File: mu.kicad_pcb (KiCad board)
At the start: 4 copper layers, 60 x 60 mm, 80 parts, among them J1 JTAG-10 PIN, J2 XT30PW-M, J5 ESQ-110-X-X-D, U1 STM32F042F6P6, U10 TLV3603QDCKRQ1, U11 SN74LVC1G74DCUT, U12 LM4040AIM3-2.5/NOPB, U13 MCP4921-E/SN, U14 BMP390, U2 MAX5026EUT_T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

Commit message: fixed the connector
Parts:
- removed C32: 100nF, Resistor_SMD:R_0402_1005Metric
- removed R16: 2.49KΩ 0.1%, Resistor_SMD:R_0402_1005Metric
- removed U12: LM4040AIM3-2.5/NOPB, footprints:DBZ3
- added J3: U.FL-R-SMT-1_10_, footprints:HRS_U.FL-R-SMT-1_10_, B.Cu at (159.2, 75.0)
- added R7: 0Ω, Resistor_SMD:R_0402_1005Metric, B.Cu at (154.0, 73.0)
- added R8: 50Ω 0.1%, Resistor_SMD:R_0402_1005Metric, B.Cu at (156.0, 72.9)
- R1: value 220K -> 210K
- moved R3 0.37 mm to (154.8, 74.8)
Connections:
- J2 pad N: Net-(MOSFET1-D) -> GND
- J2 pad P: GND -> Net-(MOSFET1-D)
- J5 pad 01: 5v_SERVO -> unconnected-(J5-Pad01)
- J5 pad 02: 5v_SERVO -> unconnected-(J5-Pad02)
- J5 pad 09: NRST1 -> unconnected-(J5-Pad09)
- J5 pad 10: NRST2 -> unconnected-(J5-Pad10)
- J5 pad 11: NRST3 -> unconnected-(J5-Pad11)
- J5 pad 12: NRST4 -> unconnected-(J5-Pad12)
- J5 pad 13: NRST5 -> unconnected-(J5-Pad13)
- R3 pad 1: 2.5V_Ref -> GND
- Rg1 pad 2: 2.5V_Ref -> GND
- U3 pad 1: 2.5V_Ref -> GND
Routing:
- net 2.5V_Ref: track 12.5 -> 0.00 mm, vias 1 -> 0
- net Net-(MOSFET1-D): track 13.7 -> 8.46 mm
- net Net-(J3-Pad2): track 0.00 -> 2.92 mm
- net 5V: track 92.4 -> 89.7 mm
- net CAN_+: track 11.6 -> 13.4 mm
- net Net-(U10-IN+): track 10.6 -> 12.0 mm
- net Net-(R7-Pad2): track 0.00 -> 0.97 mm
- net GND: track 43.7 -> 42.9 mm, vias 67 -> 69

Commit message: fixed the connector
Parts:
- removed R5: 10K, Resistor_SMD:R_0402_1005Metric
- moved C13 0.82 mm to (159.0, 82.7)
- moved C9 0.41 mm to (162.0, 82.7)
- moved C8 0.40 mm to (161.0, 82.7)
- moved FB1 0.36 mm to (160.0, 82.7)
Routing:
- net NRST: track 24.1 -> 22.9 mm
- net GND: track 42.9 -> 42.4 mm

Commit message: major revisions
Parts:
- added C32: 8pF, Capacitor_SMD:C_0402_1005Metric, B.Cu at (160.3, 81.4)
- added C33: 8pF, Capacitor_SMD:C_0402_1005Metric, B.Cu at (155.5, 81.4)
- added XTAL1: NX3225GD-8MHZ-STD-CRA-3, footprints:XTAL_NX3225GD-8MHZ-STD-CRA-3_NDK, B.Cu at (157.9, 82.0)
- moved C13 5.57 mm to (155.8, 87.3)
- moved FB1 2.32 mm to (161.8, 81.2), turned to 180 degrees
- moved C8 0.95 mm to (161.8, 83.3), turned to 0 degrees
- moved R6 0.67 mm to (155.8, 84.8), turned to 180 degrees
- moved C9 0.55 mm to (161.8, 82.2), turned to 0 degrees
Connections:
- U1 pad 2: unconnected-(U1A-PF0-OSC_IN-Pad2) -> Net-(U1A-PF0-OSC_IN)
- U1 pad 3: unconnected-(U1A-PF1-OSC_OUT-Pad3) -> Net-(U1A-PF1-OSC_OUT)
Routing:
- net Net-(U1A-PF0-OSC_IN): track 0.00 -> 4.73 mm
- net Net-(U1A-PF1-OSC_OUT): track 0.00 -> 4.39 mm
- net GND: track 42.4 -> 39.6 mm, vias 69 -> 72
- net 3.3V_Dig: track 132.2 -> 130.7 mm
- net HV: track 31.1 -> 32.0 mm
- net Net-(U1B-VDDA): track 4.65 -> 5.44 mm
- net NRST: track 22.9 -> 23.7 mm

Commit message: added the label
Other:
- board text added: "Mu v1.0"
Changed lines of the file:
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@@
+		)
+	)
+	(gr_text "Mu\nv1.0"
+		(at 176.28221 82.813514 0)
+		(layer "B.SilkS")
+		(effects
+			(font
+				(face "Arial")
+				(size 2 2)
+				(thickness 0.1)
+			)
+			(justify left bottom mirror)
+		)
+		(render_cache "Mu\nv1.0" 0
+			(polygon
+				(pts
+					(xy 176.074481 79.113514) (xy 176.074481 77.10486) (xy 175.675632 77.10486) (xy 175.201557 78.523056)
+					(xy 175.105936 78.819445) (xy 174.999324 78.498388) (xy 174.519753 77.10486) (xy 174.163159 77.10486)
+					(xy 174.163159 79.113514) (xy 174.418637 79.113514) (xy 174.418637 77.433123) (xy 175.000667 79.113514)
+					(xy 175.239781 79.113514) (xy 175.819003 77.409675) (xy 175.819003 79.113514)
+				)
+			)
+			(polygon
+				(pts
+					(xy 172.815793 79.113514) (xy 172.815793 78.899557) (xy 172.890296 78.989736) (xy 172.972277 79.057517)
+					(xy 173.062645 79.105462) (xy 173.163138 79.134688) (xy 173.276191 79.144777) (xy 173.401171 79.132312)
+					(xy 173.516037 79.095562) (xy 173.615918 79.037799) (xy 173.681267 78.971853) (xy 173.726361 78.890946)
+					(xy 173.757105 78.789281) (xy 173.767634 78.706156) (xy 173.772126 78.559571) (xy 173.772126 77.65978)
+					(xy 173.526295 77.65978) (xy 173.526295 78.465781) (xy 173.521536 78.643117) (xy 173.511274 78.725778)
+					(xy 173.48961 78.786753) (xy 173.457008 78.837032) (xy 173.412967 78.878308) (xy 173.360314 78.908496)
+					(xy 173.299047 78.927186) (xy 173.227098 78.933751) (xy 173.120073 78.919608) (xy 173.019491 78.876964)
+					(xy 172.960342 78.833883) (xy 172.91503 78.782655) (xy 172.882105 78.722359) (xy 172.853447 78.612983)
+					(xy 172.841805 78.438426) (xy 172.841805 77.65978) (xy 172.595852 77.65978) (xy 172.595852 79.113514)
+				)
+			)
+			(polygon
+				(pts
+					(xy 175.694683 82.473514) (xy 176.246672 81.01978) (xy 175.987042 81.01978) (xy 175.675632 81.890384)
+					(xy 175.582698 82.183353) (xy 175.491107 81.90687) (xy 175.168706 81.01978) (xy 174.915915 81.01978)
+					(xy 175.465217 82.473514)
+				)
+			)
+			(polygon
+				(pts
+					(xy 173.840758 82.473514) (xy 174.086711 82.473514) (xy 174.086711 80.902299) (xy 174.18458 80.983728)
+					(xy 174.319596 81.07217) (xy 174.461686 81.149053) (xy 174.578494 81.199543) (xy 174.578494 80.961162)
+					(xy 174.444695 80.890574) (xy 174.324853 80.81203) (xy 174.217869 80.72559) (xy 174.119721 80.628483)
+					(xy 174.048319 80.539349) (xy 173.999272 80.457045) (xy 173.840758 80.457045)
+				)
+			)
+			(polygon
+				(pts
+					(xy 173.073713 82.473514) (xy 173.073713 82.199962) (xy 172.793689 82.199962) (xy 172.793689 82.473514)
+				)
+			)
+			(polygon
+				(pts
+					(xy 171.922484 80.470966) (xy 172.041919 80.510571) (xy 172.143759 80.57477) (xy 172.22937 80.660992)
+					(xy 172.301905 80.771021) (xy 172.361013 80.909138) (xy 172.399037 81.055679) (xy 172.424592 81.243698)
+					(xy 172.434041 81.481643) (xy 172.423903 81.721152) (xy 172.396095 81.915881) (xy 172.353981 82.072761)
+					(xy 172.300085 82.19797) (xy 172.23596 82.296804) (xy 172.145916 82.387472) (xy 172.042129 82.451586)
+					(xy 171.921867 82.490988) (xy 171.780936 82.504777) (xy 171.638529 82.49076) (xy 171.518722 82.450932)
+					(xy 171.416892 82.386441) (xy 171.331307 82.299761) (xy 171.259019 82.189469) (xy 171.200371 82.05134)
+					(xy 171.162618 81.904773) (xy 171.137298 81.717588) (xy 171.127953 81.481643) (xy 171.127986 81.480911)
+					(xy 171.380622 81.480911) (xy 171.390748 81.743691) (xy 171.416816 81.929282) (xy 171.453289 82.055465)
+					(xy 171.496149 82.137435) (xy 171.560378 82.212222) (xy 171.628308 82.262387) (xy 171.701102 82.291695)
+					(xy 171.780936 82.301567) (xy 171.860813 82.29173) (xy 171.933646 82.262532) (xy 172.001602 82.212582)
+					(xy 172.065845 82.138168) (xy 172.108612 82.056488) (xy 172.145048 81.930394) (xy 172.171116 81.744528)
+					(xy 172.18125 81.480911) (xy 172.170483 81.21971) (xy 172.142388 81.029669) (xy 172.10235 80.895453)
+					(xy 172.054244 80.803869) (xy 171.998117 80.739865) (xy 171.935383 80.695816) (xy 171.864686 80.669369)
+					(xy 171.783623 80.660255) (xy 171.702305 80.670128) (xy 171.628592 80.699344) (xy 171.560272 80.749136)
+					(xy 171.496149 80.823042) (xy 171.453383 80.904392) (xy 171.416908 81.030355) (xy 171.390785 81.216463)
+					(xy 171.380622 81.480911) (xy 171.127986 81.480911) (xy 171.140732 81.198756) (xy 171.173016 81.00769)
+					(xy 171.22838 80.841029) (xy 171.297335 80.70947) (xy 171.355601 80.633407) (xy 171.422341 80.571328)
+					(xy 171.498225 80.522013) (xy 171.581502 80.486612) (xy 171.675087 80.464678) (xy 171.780936 80.457045)
+				)
+			)
 		)
 	)

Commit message: drc pass
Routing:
- net GND: track 39.6 -> 40.9 mm
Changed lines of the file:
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@@
 		(tenting front back)
 		(pcbplotparams
-			(layerselection 0x00000000_00000000_55555555_5755f5ff)
+			(layerselection 0x00000000_00000000_55555555_5755f55f)
 			(plot_on_all_layers_selection 0x00000000_00000000_00000000_00000000)
 			(disableapertmacros no)
@@
 			(at 1.27 6.1 90)
 			(layer "B.SilkS")
+			(hide yes)
 			(effects
 				(font
@@
 			(at -9.825 3.635 90)
 			(layer "B.SilkS")
+			(hide yes)
 			(effects
 				(font
@@
 	)
 	(segment
+		(start 160.4 80.821635)
+		(end 160.321668 80.899967)
+		(width 0.2)
+		(layer "B.Cu")
+		(net 1)
+	)
+	(segment
 		(start 160.3 92.464001)
 		(end 160.414999 92.579)
@@
 		(layer "B.Cu")
 		(net 1)
+	)
+	(segment
+		(start 160.4 79.649454)
+		(end 160.4 80.821635)
+		(width 0.2)
+		(layer "B.Cu")
+		(net 1)

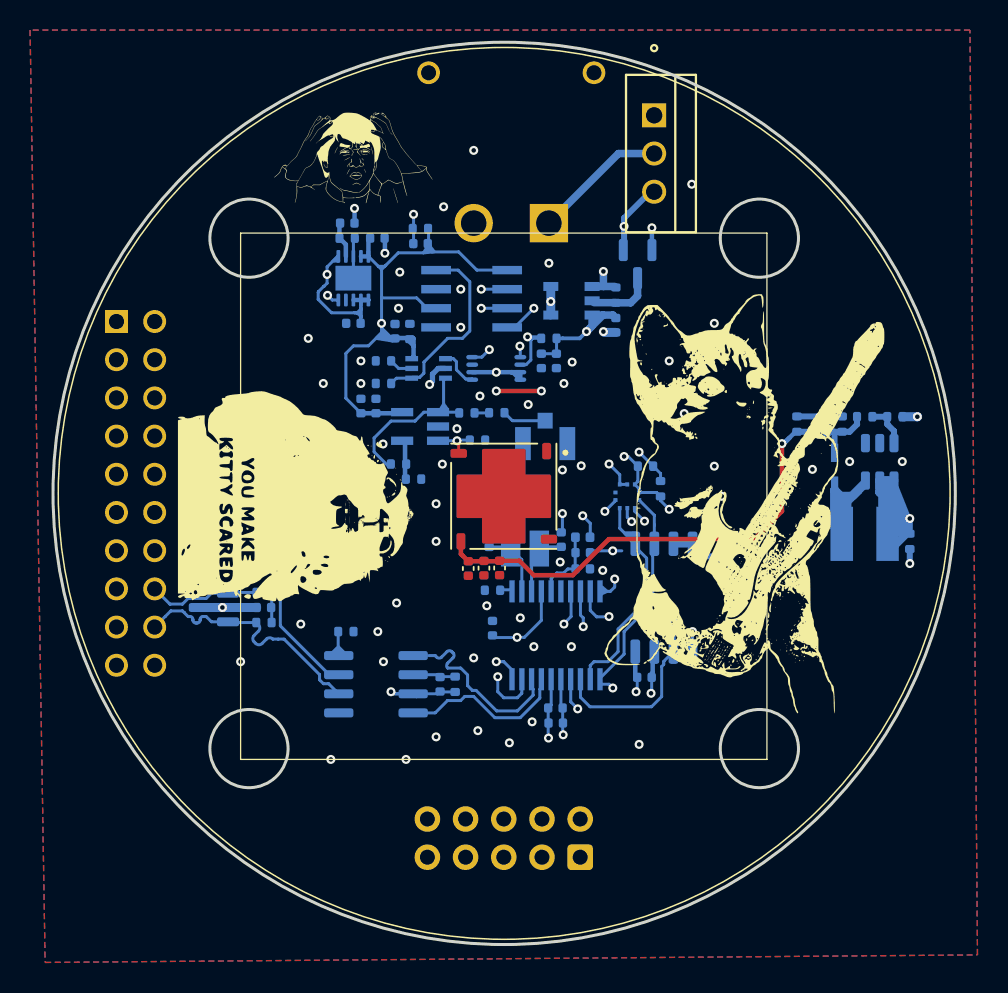
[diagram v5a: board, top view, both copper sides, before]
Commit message: thermal expansion vias
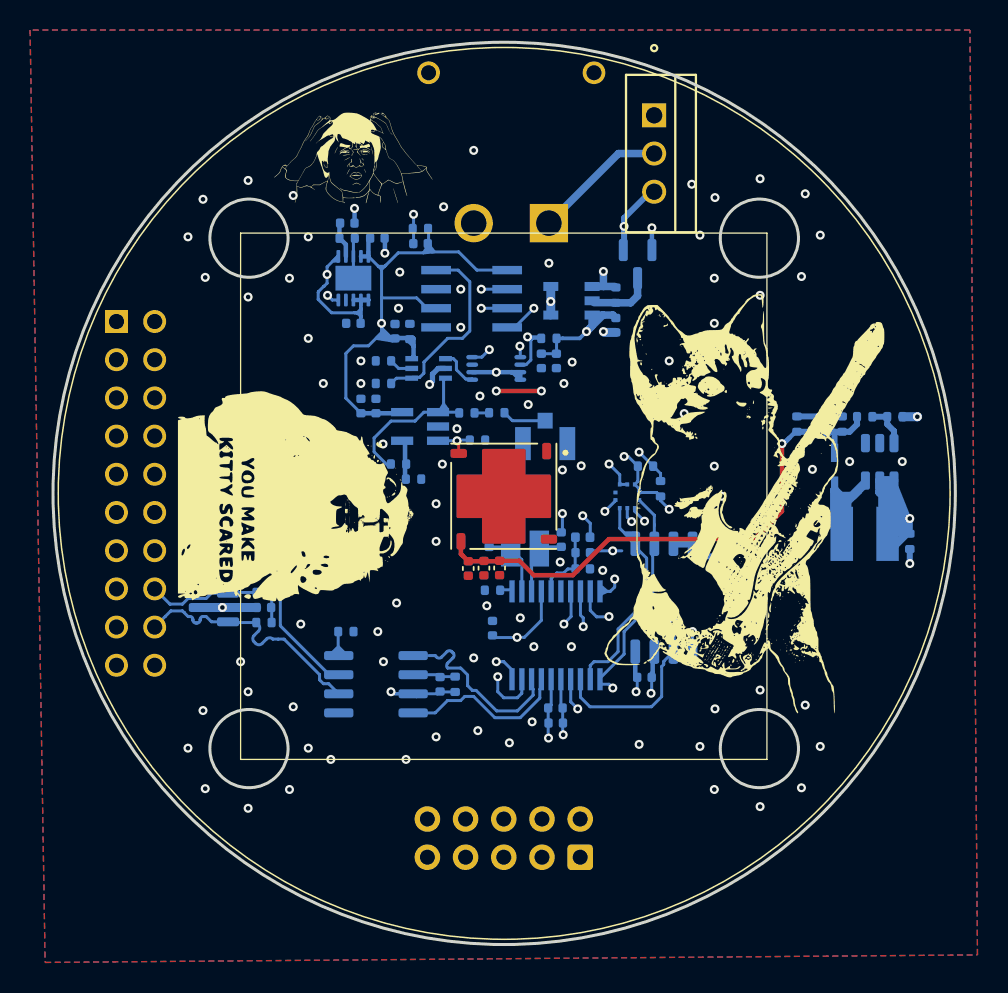
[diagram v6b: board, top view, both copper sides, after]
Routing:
- net 5V_LOGIC: track 44.5 -> 45.5 mm
- net GND: vias 72 -> 104
